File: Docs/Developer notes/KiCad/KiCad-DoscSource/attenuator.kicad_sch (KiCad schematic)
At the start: 8 parts, among them SW1 SW_SP3T

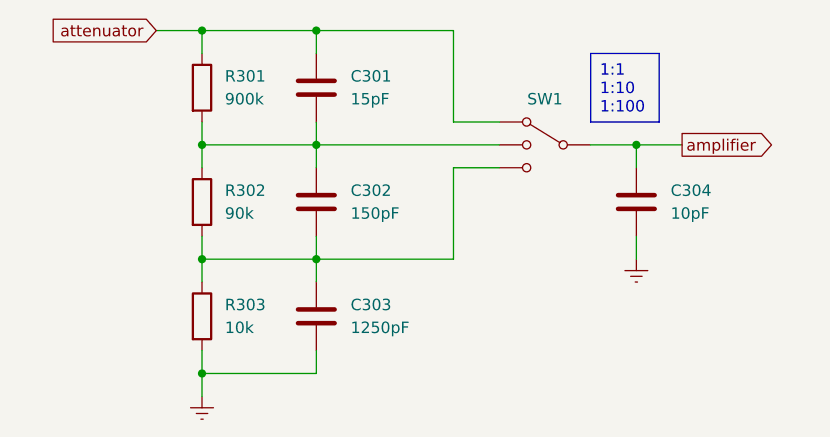
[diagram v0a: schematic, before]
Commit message: Add attenuator to developer notes
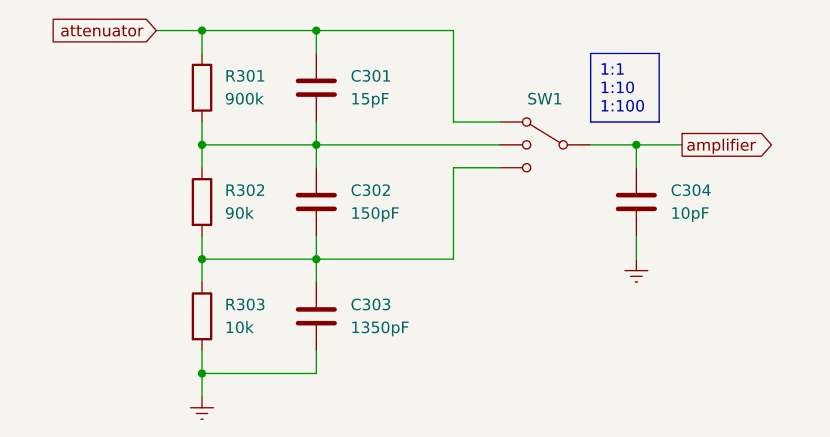
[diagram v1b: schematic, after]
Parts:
- C303: value 1250pF -> 1350pF
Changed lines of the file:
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@@
       (effects (font (size 1.27 1.27)) (justify left))
     )
-    (property "Value" "1250pF" (at 34.29 35.56 0)
+    (property "Value" "1350pF" (at 34.29 35.56 0)
       (effects (font (size 1.27 1.27)) (justify left))
     )
